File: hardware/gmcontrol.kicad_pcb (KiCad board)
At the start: 2 copper layers, 116 parts, among them J1 USB_OTG, J2 Jack-DC, J3 Conn_01x18, J4 Screw_Terminal_01x04, Q1 BC817, Q10 BC817, Q11 BC817, Q12 BC807, Q13 BC817, Q14 BC807, Q15 AON7212, Q16 AON7212, Q17 BC817, Q18 BC817, Q19 BC817, Q2 BC817, Q20 BC807, Q21 BC817, Q22 BC807, Q23 AON7212, Q24 AON7212, Q25 BC817, Q26 BC817, Q27 BC817, Q28 BC807, Q29 BC817, Q3 BC817, Q30 BC807, Q31 AON7212, Q32 AON7212, Q33 BSS138, Q34 BC817, Q35 BSS84, Q36 AO3401, Q4 BC807, Q5 BC817, Q6 BC807, Q7 AON7212, Q8 AON7212, Q9 BC817, U1 STM32F103C8Tx, U2 HT7333-1, Y1 16Mhz

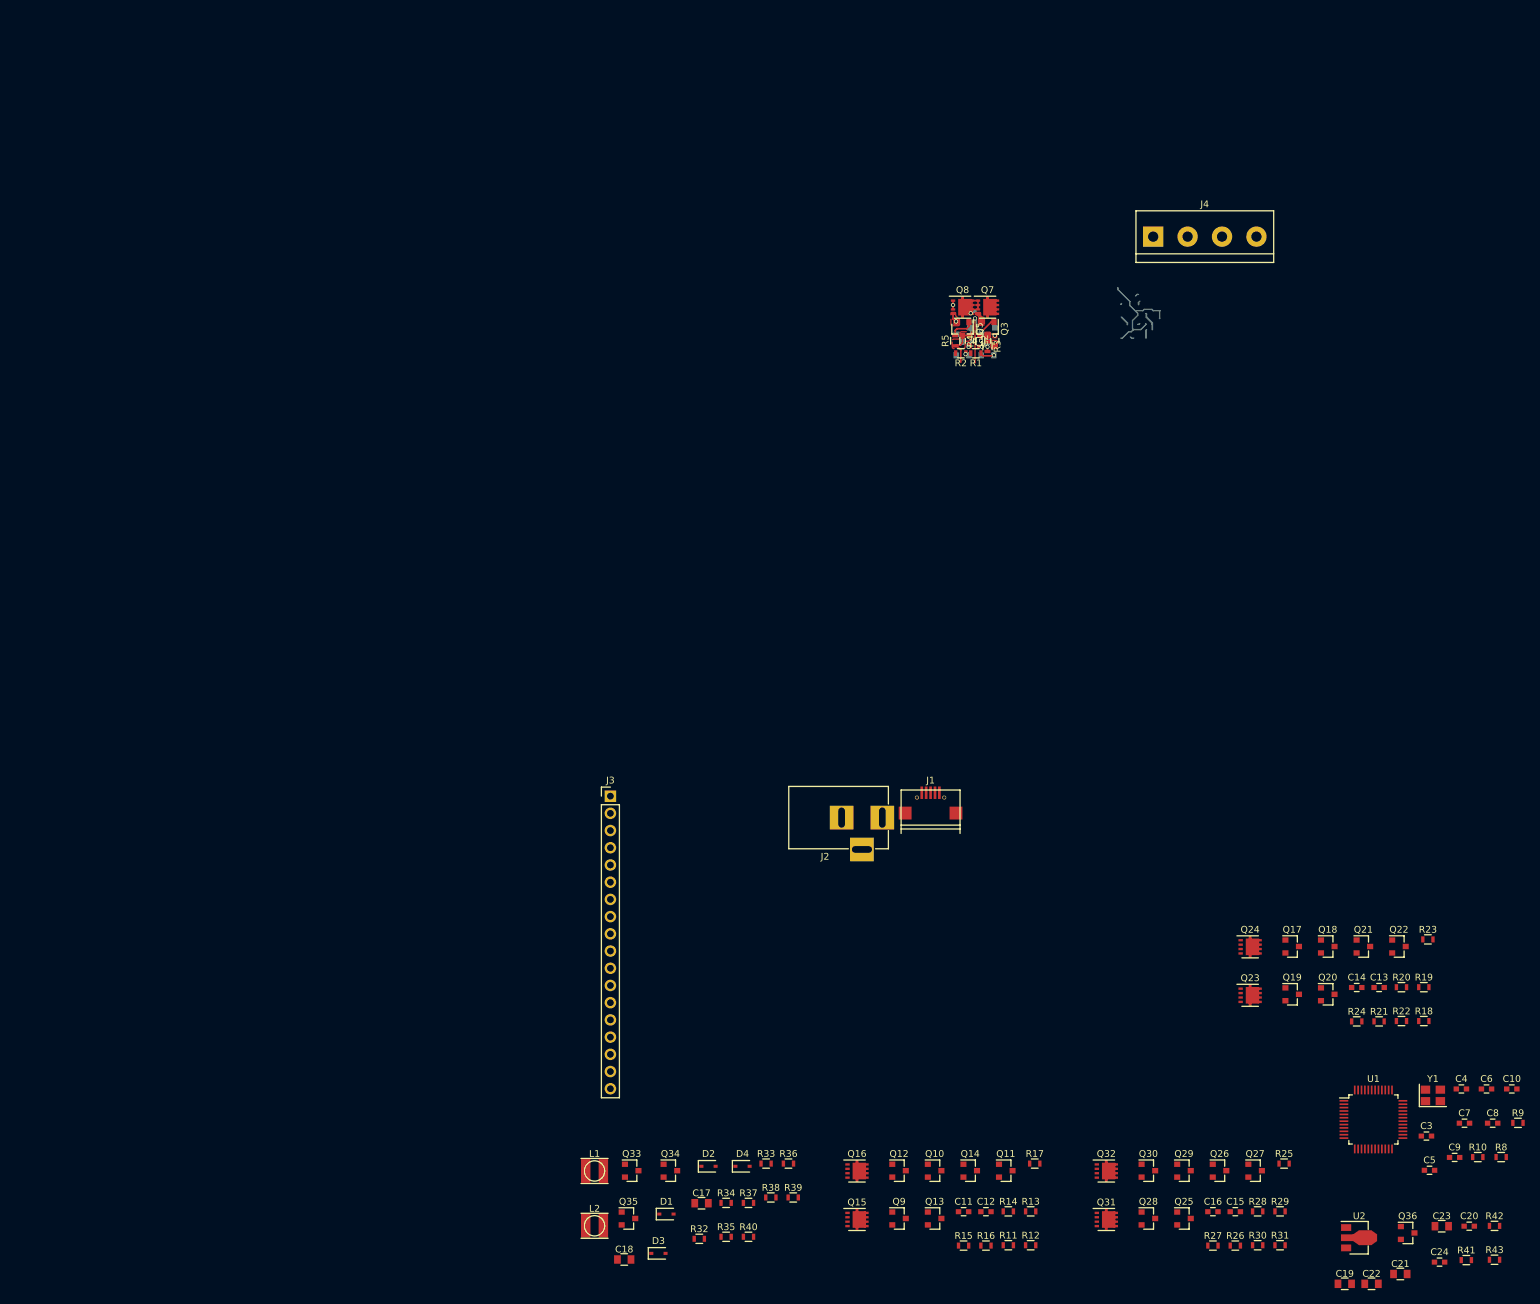
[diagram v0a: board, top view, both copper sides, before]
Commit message: change to kicad 5
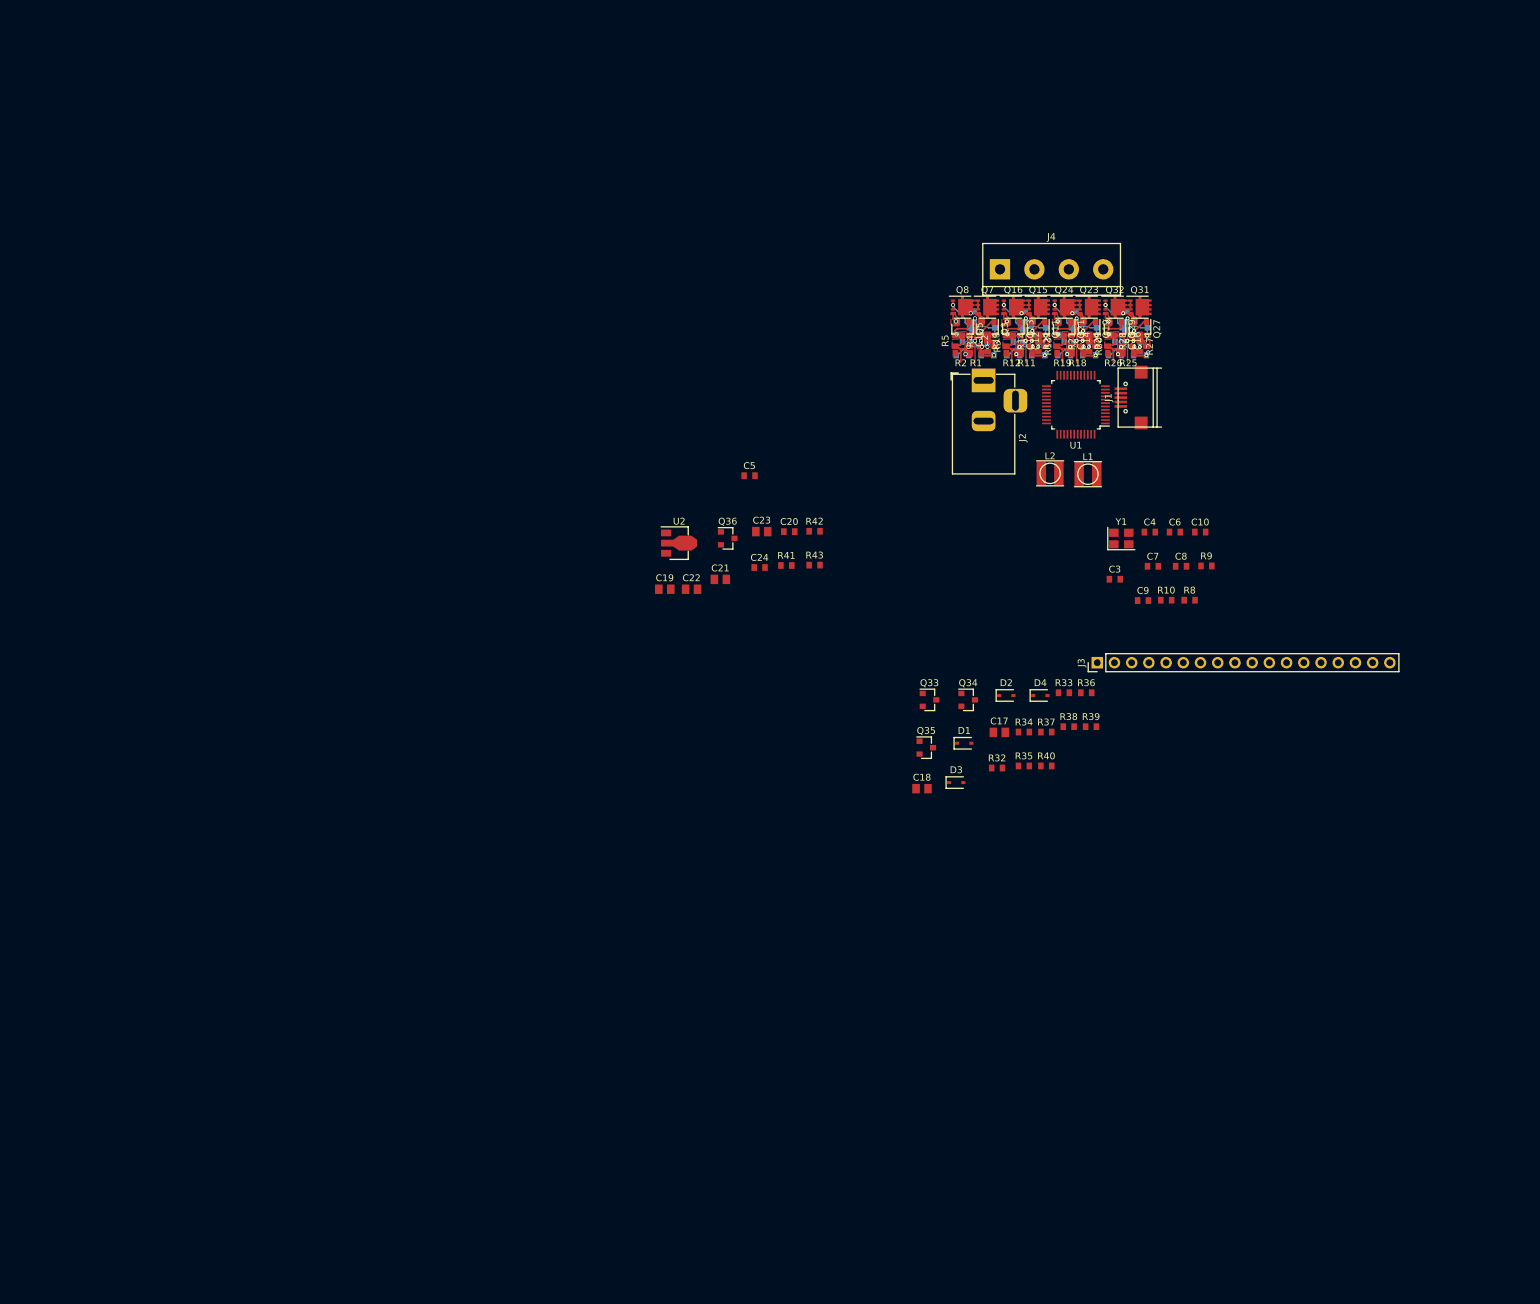
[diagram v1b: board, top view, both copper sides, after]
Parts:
- C1, C10, C11, C12, C13, C14, C15, C16, C2, C20, C24, C3, C4, C5, C6, C7, C8, C9: footprint Capacitors_SMD:C_0603 -> Capacitor_SMD:C_0603_1608Metric
- C17, C18, C19, C21, C22, C23: footprint Capacitors_SMD:C_0805 -> Capacitor_SMD:C_0805_2012Metric
- D1, D2, D3, D4: footprint Diodes_SMD:D_SOD-323 -> Diode_SMD:D_SOD-323
- J2: footprint Connectors:BARREL_JACK -> Connector_BarrelJack:BarrelJack_Horizontal
- J3: footprint Pin_Headers:Pin_Header_Straight_1x18_Pitch2.54mm -> Connector_PinHeader_2.54mm:PinHeader_1x18_P2.54mm_Vertical
- J4: footprint Connectors_Terminal_Blocks:TerminalBlock_bornier-4_P5.08mm -> TerminalBlock:TerminalBlock_bornier-4_P5.08mm
- Q1, Q11, Q13, Q19, Q2, Q21, Q27, Q29, Q3, Q33, Q34, Q35, Q36, Q4, Q5, Q6: footprint TO_SOT_Packages_SMD:SOT-23 -> Package_TO_SOT_SMD:SOT-23
- Q10, Q12, Q14, Q17, Q18, Q20, Q22, Q25, Q26, Q28, Q30, Q9: footprint TO_SOT_Packages_SMD:SOT-23 -> Package_TO_SOT_SMD:SOT-23; moved to B.Cu
- R1, R10, R11, R12, R13, R14, R15, R18, R19, R2, R20, R21, R22, R25, R26, R27, R28, R29, R3, R32, R33, R34, R35, R36, R37, R38, R39, R4, R40, R41, R42, R43, R5, R6, R7, R8, R9: footprint Resistors_SMD:R_0603 -> Resistor_SMD:R_0603_1608Metric
- R16, R17, R23, R24, R30, R31: footprint Resistors_SMD:R_0603 -> Resistor_SMD:R_0603_1608Metric; moved to B.Cu
- U1: footprint Housings_QFP:LQFP-48_7x7mm_Pitch0.5mm -> Package_QFP:LQFP-48_7x7mm_P0.5mm
- U2: footprint TO_SOT_Packages_SMD:SOT-89-3 -> Package_TO_SOT_SMD:SOT-89-3
- Y1: footprint Crystals:Crystal_SMD_3225-4pin_3.2x2.5mm -> Crystal:Crystal_SMD_3225-4Pin_3.2x2.5mm
- moved C20 143.4 mm to (214.3, 86.5)
- moved C21 143.4 mm to (204.1, 93.5)
- moved C22 143.4 mm to (199.9, 95.0)
- moved C24 143.4 mm to (209.9, 91.8)
- moved C5 143.4 mm to (208.4, 78.2)
- moved R42 143.4 mm to (218.0, 86.4)
- moved R43 143.4 mm to (218.0, 91.4)
- moved U2 143.4 mm to (197.6, 88.2)
- moved C19 143.4 mm to (195.9, 95.0)
- moved C23 143.4 mm to (210.2, 86.5)
- moved Q36 143.4 mm to (205.2, 87.5)
- moved R41 143.4 mm to (213.8, 91.5)
- moved R30 138.4 mm to (264.0, 54.7), turned to 90 degrees
- moved Q15 137.2 mm to (251.0, 53.3)
- moved R16 137.2 mm to (249.0, 54.7), turned to 90 degrees
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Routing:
- net /controller/GND: track 2.88 -> 81.1 mm, vias 4 -> 16
- net (no net): track 25.2 -> 0.00 mm
- net /gate_voltage_supply/Vgl: track 6.33 -> 25.3 mm
- net /sheet5AEA3194/SENSE: track 0.00 -> 8.01 mm, vias 0 -> 2
- net /sheet5AEA2A39/SENSE: track 0.00 -> 8.01 mm, vias 0 -> 2
- net /sheet5AEA1DE6/SENSE: track 0.00 -> 8.01 mm, vias 0 -> 2
- net /sheet5AEA1DE6/PHASE: track 0.00 -> 7.32 mm, vias 0 -> 1
- net /sheet5AEA3194/PHASE: track 0.00 -> 7.32 mm, vias 0 -> 1
- net /sheet5AEA2A39/PHASE: track 0.00 -> 7.32 mm, vias 0 -> 1
- net /gate_voltage_supply/Vgh: track 2.43 -> 9.70 mm
- net Net-(Q25-Pad3): track 0.00 -> 5.79 mm, vias 0 -> 2
- net Net-(Q17-Pad3): track 0.00 -> 5.79 mm, vias 0 -> 2
- net Net-(Q11-Pad1): track 0.00 -> 5.79 mm, vias 0 -> 2
- net Net-(Q18-Pad3): track 0.00 -> 5.34 mm, vias 0 -> 1
- net Net-(Q10-Pad3): track 0.00 -> 5.34 mm, vias 0 -> 1
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- added copper zone on F.Cu, net Net-(Q11-Pad2)
- added copper zone on F.Cu, net Net-(Q13-Pad2)
- added copper zone on F.Cu, net Net-(Q19-Pad2)
- added copper zone on F.Cu, net Net-(Q21-Pad2)
- added copper zone on F.Cu, net Net-(Q27-Pad2)
- added copper zone on F.Cu, net Net-(Q29-Pad2)

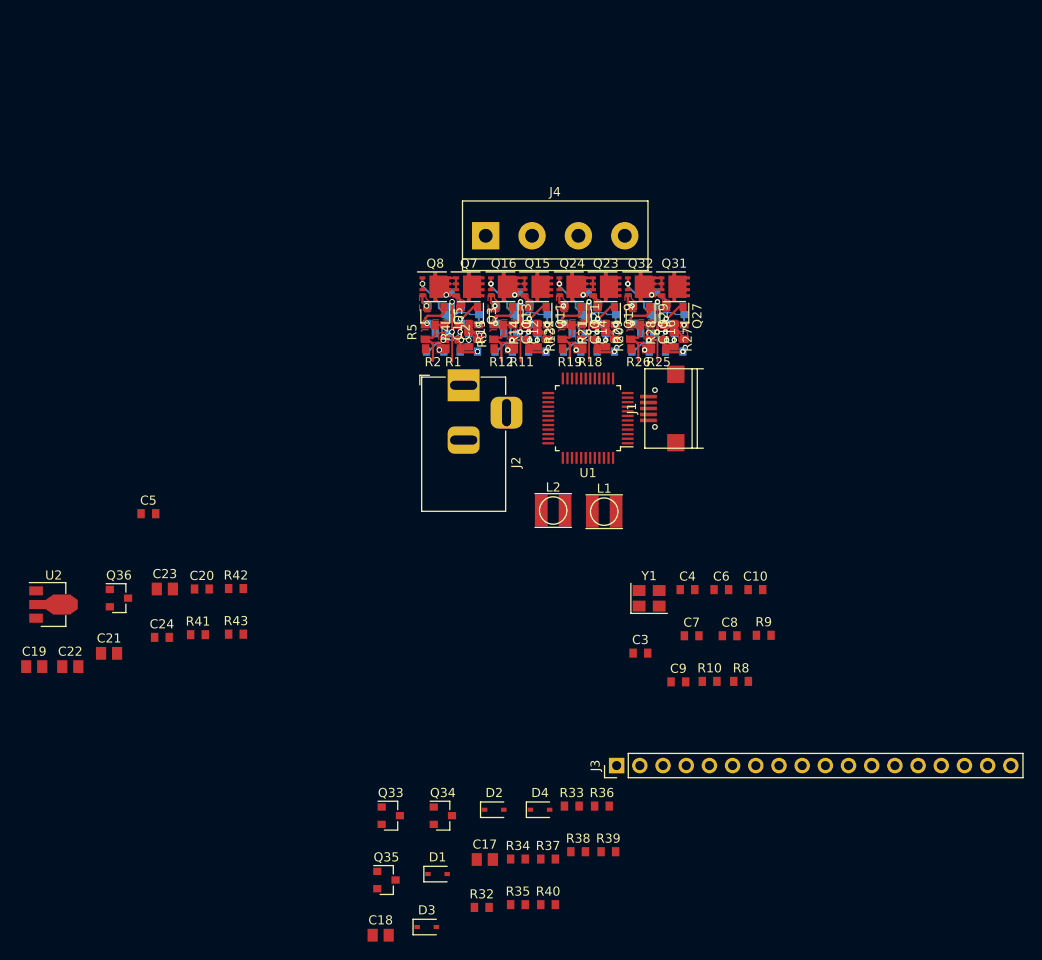
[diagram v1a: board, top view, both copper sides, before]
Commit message: smaller footprints
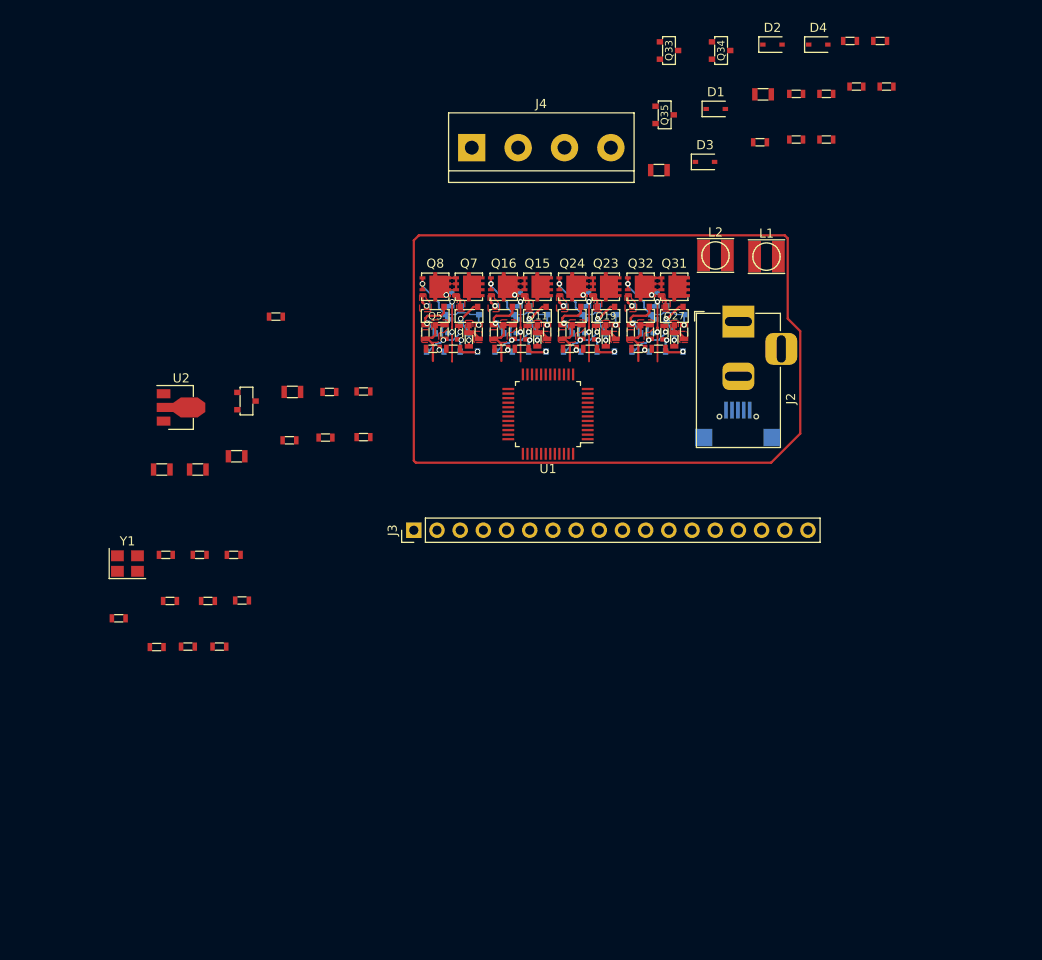
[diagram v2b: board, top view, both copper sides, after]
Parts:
- C1, C10, C11, C12, C13, C14, C15, C16, C2, C20, C24, C3, C4, C5, C6, C7, C8, C9: footprint Capacitor_SMD:C_0603_1608Metric -> _Generic:0603_Small
- C17, C18, C19, C21, C22, C23: footprint Capacitor_SMD:C_0805_2012Metric -> _Generic:0805_Small
- J1: moved to B.Cu
- Q1, Q10, Q11, Q12, Q13, Q14, Q17, Q18, Q19, Q2, Q20, Q21, Q22, Q25, Q26, Q27, Q28, Q29, Q3, Q30, Q33, Q34, Q35, Q36, Q4, Q5, Q6, Q9: footprint Package_TO_SOT_SMD:SOT-23 -> _Generic:SOT-23_Small
- Q15, Q16, Q23, Q24, Q31, Q32, Q7, Q8: footprint gmcontrol:DFN3x3A_8L_EP1_P -> _Generic:DFN3x3A_8L_EP1_P
- R1, R10, R11, R12, R13, R14, R15, R16, R17, R18, R19, R2, R20, R21, R22, R23, R24, R25, R26, R27, R28, R29, R3, R30, R31, R32, R33, R34, R35, R36, R37, R38, R39, R4, R40, R41, R42, R43, R5, R6, R7, R8, R9: footprint Resistor_SMD:R_0603_1608Metric -> _Generic:0603_Small
- moved D1 89.2 mm to (270.6, 33.9)
- moved D3 89.2 mm to (269.4, 39.7)
- moved R33 89.2 mm to (285.3, 26.4)
- moved R38 89.2 mm to (286.0, 31.4)
- moved R39 89.2 mm to (289.3, 31.4)
- moved C18 89.2 mm to (264.3, 40.6)
- moved D2 89.2 mm to (276.8, 26.8)
- moved D4 89.2 mm to (281.8, 26.8)
- moved Q33 89.2 mm to (265.4, 27.5)
- moved Q34 89.2 mm to (271.2, 27.5)
- moved Q35 89.2 mm to (265.0, 34.5)
- moved R32 89.2 mm to (275.4, 37.5)
- moved R34 89.2 mm to (279.4, 32.2)
- moved R35 89.2 mm to (279.4, 37.2)
- moved R36 89.2 mm to (288.6, 26.4)
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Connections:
- J1 pad 4: Net-(J1-Pad4) -> (no net)
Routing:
- net (no net): track 0.00 -> 131.2 mm

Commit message: motor layout
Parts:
- removed J3: Conn_01x18, Connector_PinHeader_2.54mm:PinHeader_1x18_P2.54mm_Vertical
- removed J4: Screw_Terminal_01x04, TerminalBlock:TerminalBlock_bornier-4_P5.08mm
- C19, C21, C23: moved to B.Cu
- J1, Q1, Q10, Q12, Q14, Q2, Q25, Q26, Q28, Q30, Q4, Q6, Q9, R16, R17, R24, R30, R31, R6, R7: moved to F.Cu
- moved C17 173.0 mm to (115.8, 98.0)
- moved R36 171.7 mm to (130.9, 94.4)
- moved L1 170.0 mm to (111.6, 92.9)
- moved R34 164.3 mm to (127.5, 94.8)
- moved L2 162.7 mm to (111.6, 84.8)
- moved R38 162.4 mm to (134.4, 89.5)
- moved R39 161.9 mm to (137.8, 88.6)
- moved R40 159.0 mm to (134.4, 94.4)
- moved Q33 158.9 mm to (117.2, 84.7)
- moved Q35 158.9 mm to (116.7, 91.8)
- moved D3 158.9 mm to (121.2, 96.9)
- moved D1 158.8 mm to (122.5, 91.1)
- moved Q34 158.8 mm to (123.0, 84.7)
- moved D2 158.7 mm to (128.8, 84.1)
- moved D4 158.6 mm to (133.9, 84.1)
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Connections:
- U1 pad 17: /controller/PA7 -> (no net)
- U1 pad 18: /controller/PB0 -> (no net)
- U1 pad 19: /controller/PB1 -> (no net)
- U1 pad 2: /controller/PC13 -> (no net)
- U1 pad 20: /controller/PB2 -> (no net)
- U1 pad 25: /controller/PB12 -> (no net)
- U1 pad 3: /controller/PC14 -> (no net)
- U1 pad 34: /controller/SWDIO -> (no net)
- U1 pad 37: /controller/SWDCLK -> (no net)
- U1 pad 38: /controller/PA15 -> (no net)
- U1 pad 39: /controller/PB3 -> (no net)
- U1 pad 4: /controller/PC15 -> (no net)
- U1 pad 40: /controller/PB4 -> (no net)
- U1 pad 41: /controller/PB5 -> (no net)
- U1 pad 42: /controller/PB6 -> (no net)
- U1 pad 43: /controller/PB7 -> (no net)
- U1 pad 44: /controller/BOOT0 -> (no net)
- U1 pad 7: /controller/RESET -> (no net)
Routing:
- net (no net): track 131.2 -> 0.00 mm
- net /controller/GND: track 81.1 -> 20.0 mm, vias 16 -> 7
- net /gate_voltage_supply/Vgl: track 25.3 -> 3.17 mm, vias 0 -> 1
- net /gate_voltage_supply/VIN: track 0.00 -> 10.7 mm
- net /phase_driver_1/SENSE: track 8.02 -> 0.00 mm, vias 2 -> 0
- net /sheet5AEA3194/SENSE: track 8.01 -> 0.00 mm, vias 2 -> 0
- net /sheet5AEA1DE6/SENSE: track 8.01 -> 0.00 mm, vias 2 -> 0
- net /sheet5AEA1DE6/PHASE: track 7.32 -> 0.00 mm, vias 1 -> 0
- net /phase_driver_1/PHASE: track 7.32 -> 0.00 mm, vias 1 -> 0
- net /sheet5AEA3194/PHASE: track 7.32 -> 0.00 mm, vias 1 -> 0
- net Net-(Q25-Pad3): track 5.79 -> 0.00 mm, vias 2 -> 0
- net Net-(Q11-Pad1): track 5.79 -> 0.00 mm, vias 2 -> 0
- net Net-(Q1-Pad3): track 5.79 -> 0.00 mm, vias 2 -> 0
- net Net-(Q2-Pad3): track 5.34 -> 0.00 mm, vias 1 -> 0
- net Net-(Q10-Pad3): track 5.34 -> 0.00 mm, vias 1 -> 0
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- added copper zone on B.Cu, net /controller/GND
- removed copper zone on F.Cu, net Net-(Q11-Pad2)
- removed copper zone on F.Cu, net Net-(Q13-Pad2)
- removed copper zone on F.Cu, net Net-(Q19-Pad2)
- removed copper zone on F.Cu, net Net-(Q27-Pad2)
- removed copper zone on F.Cu, net Net-(Q29-Pad2)
- removed copper zone on F.Cu, net Net-(Q3-Pad2)
- removed copper zone on F.Cu, net Net-(Q5-Pad2)
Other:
- net class Default: clearance 0.2 -> 0.15; trace_width 0.25 -> 0.15
- rule trace_clearance: 0.2 -> 0.15
